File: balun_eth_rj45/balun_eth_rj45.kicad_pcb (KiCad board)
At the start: 4 copper layers, 80 x 74 mm, 21 parts, among them J1 RJE591885401 CAT6 NO-MAGNETICS, J2 SMA_A, J3 SMA_B, J4 SMA_C, J5 SMA_D, T1 ADT2-1T+, T2 ADT2-1T+, T3 ADT2-1T+, T4 ADT2-1T+

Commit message: feat: finalize JLC parts and measurement BOM
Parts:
- J2, J3, J4, J5: footprint Connector_Coaxial:SMA_Amphenol_132289_EdgeMount -> balun_eth_rj45:SMA_MyAntenna_A-SMA-KE-16.5A_EdgeMount
- moved J2 0.30 mm to (97.8, 29.0)
- moved J3 0.30 mm to (97.8, 47.0)
- moved J4 0.30 mm to (97.8, 65.0)
- moved J5 0.30 mm to (97.8, 83.0)
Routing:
- net /GND: track 43.2 -> 82.0 mm

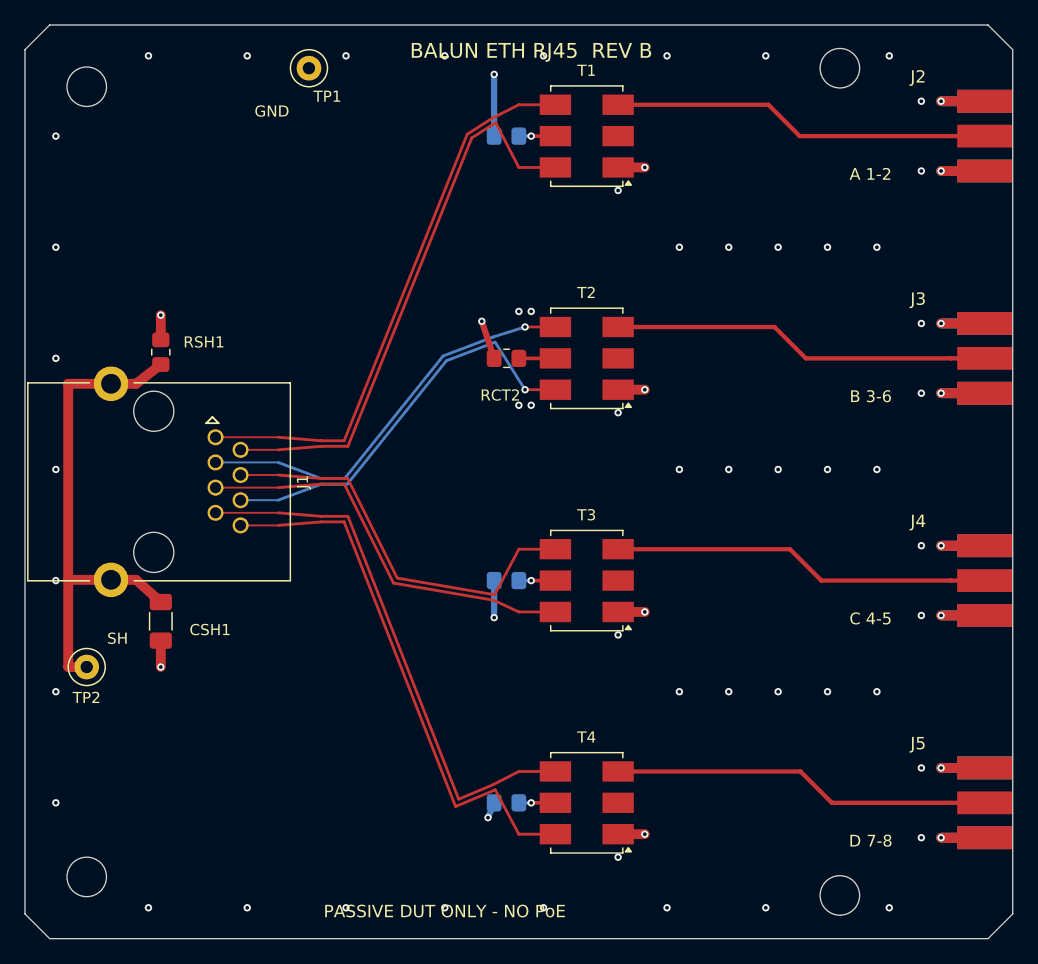
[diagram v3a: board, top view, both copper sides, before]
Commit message: Verify JLC stack impedance, update PCB widths, and document ordering options with screenshots
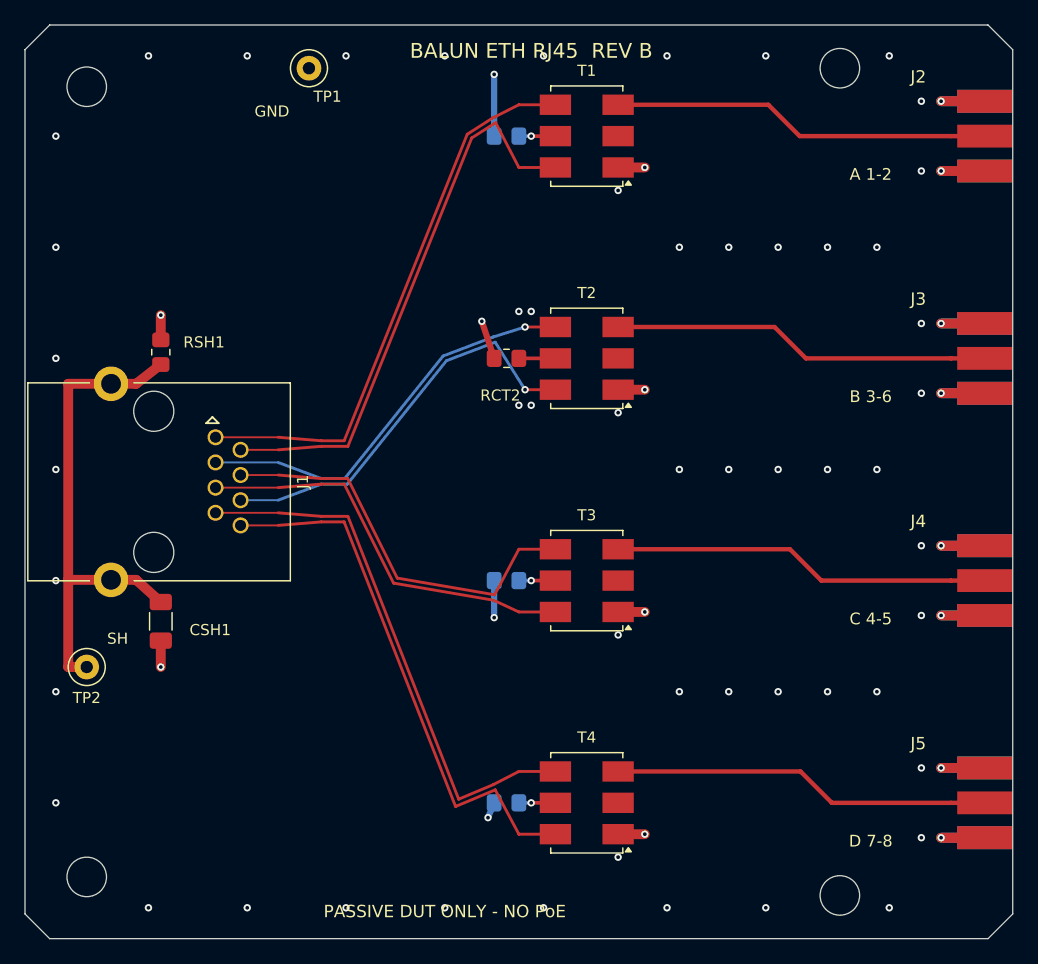
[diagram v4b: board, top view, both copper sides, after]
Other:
- board text added: "NON-COPLANAR: 50R W0.357 / 100R W0.234 G0.216"
- board text removed: "NON-COPLANAR: 50R W0.35 / 100R W0.23 G0.22"
